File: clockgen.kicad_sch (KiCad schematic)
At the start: 146 parts, among them IC3 TLV74325PDBVR, J13 73391-0083, J14 73391-0083, J15 292161-3, J16 U.FL-R-SMT-180, Q10 BSS138, Q9 BSS138, U12 AZ1117-3.3, U13 AZ1117-3.3, U14 TCA6416APWR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

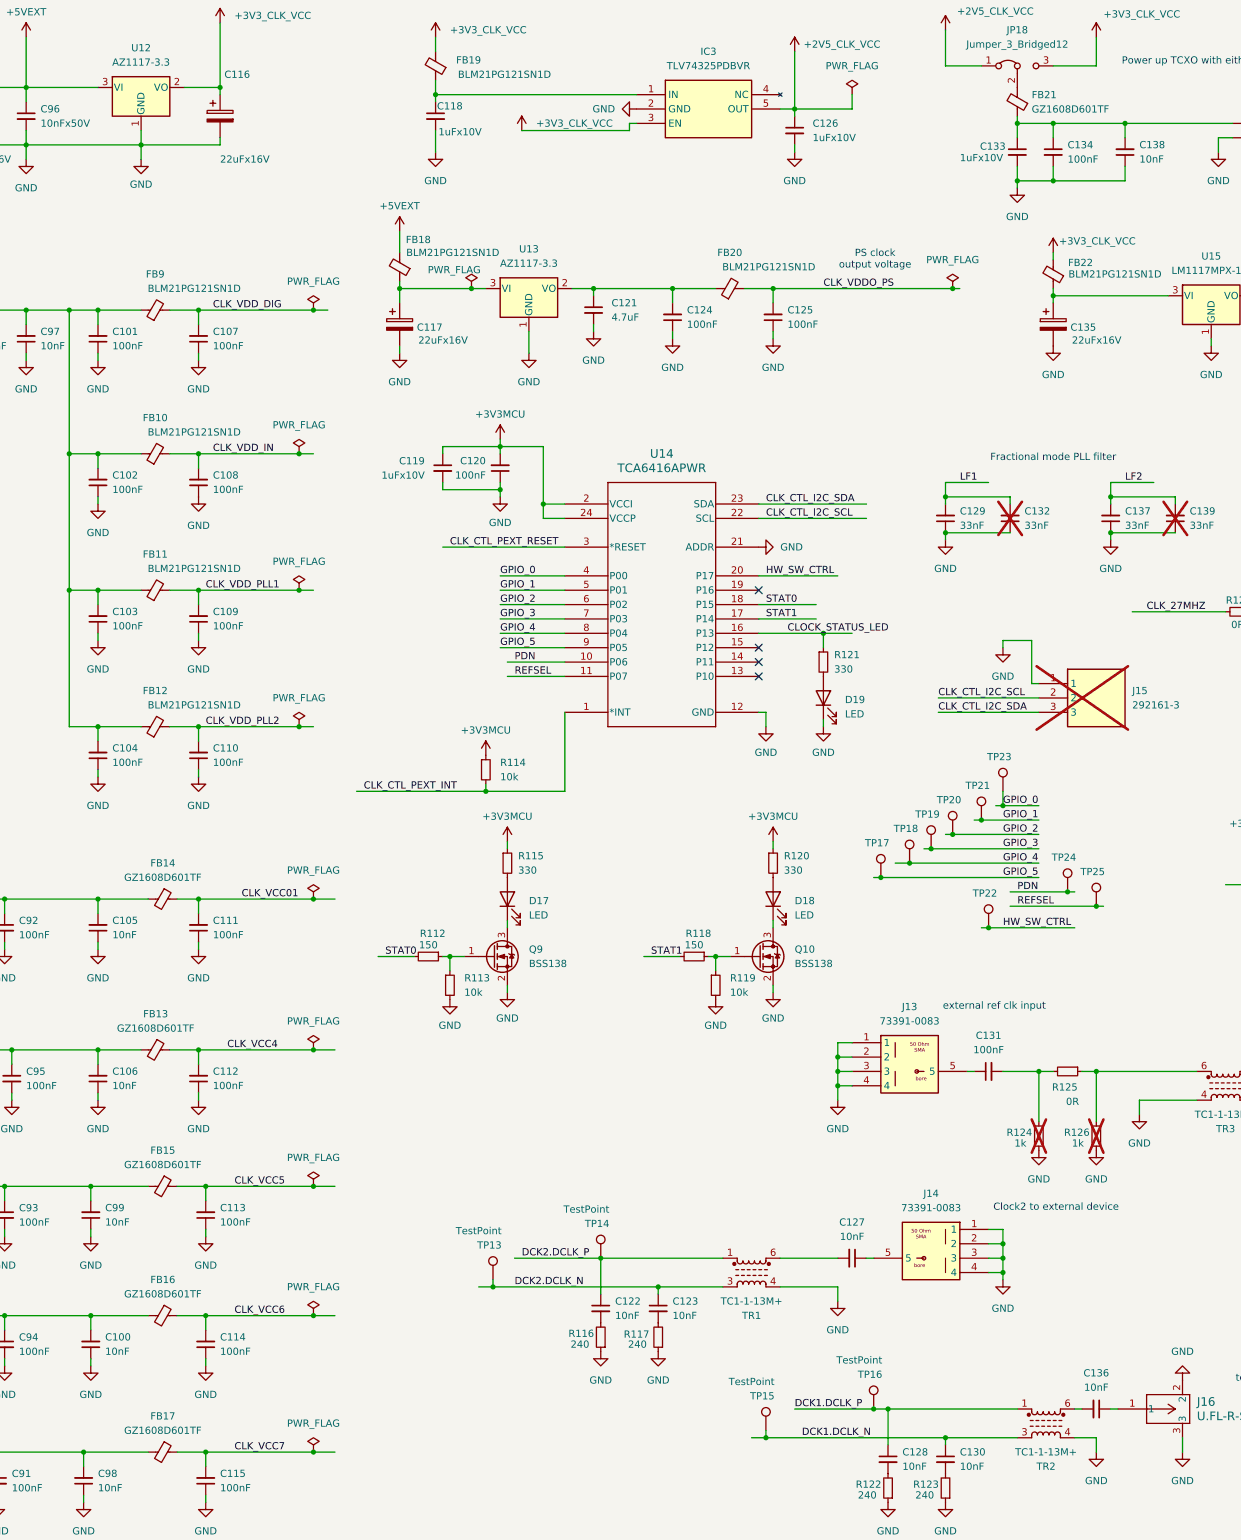
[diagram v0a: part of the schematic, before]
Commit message: JLCPCB part id's update
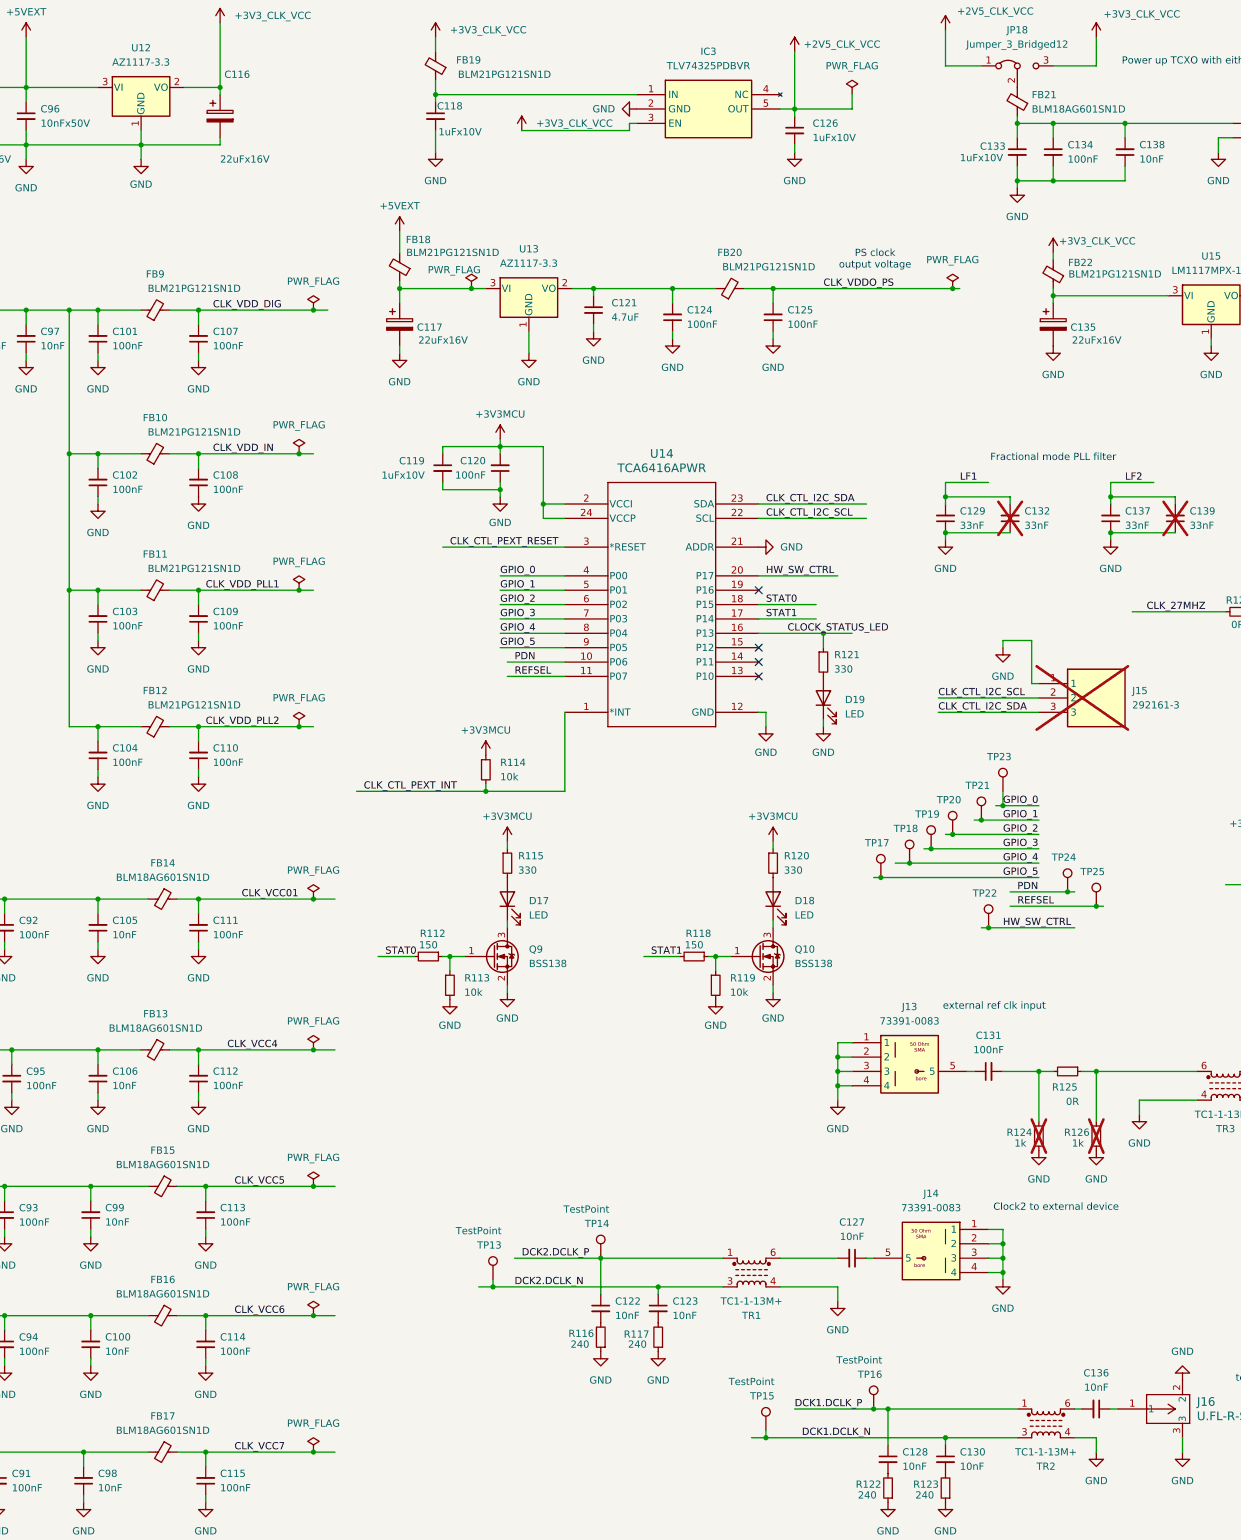
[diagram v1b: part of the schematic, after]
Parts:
- FB13, FB14, FB15, FB16, FB17, FB21: value GZ1608D601TF -> BLM18AG601SN1D; JLCPCB Part # C1002 -> C19330; Part GZ1608D601TF -> BLM18AG601SN1D
- R125, R127: JLCPCB Part # C21189 -> C2906974; Part 0603WAF0000T5E -> FRC0603F0000TS
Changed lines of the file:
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@@
 			)
 		)
-		(property "Value" "GZ1608D601TF"
+		(property "Value" "BLM18AG601SN1D"
 			(at 73.6981 167.64 90)
 			(effects
@@
 			)
 		)
-		(property "JLCPCB Part #" "C1002"
+		(property "JLCPCB Part #" "C19330"
 			(at 73.66 171.45 0)
 			(effects
@@
 			)
 		)
-		(property "Part" "GZ1608D601TF"
+		(property "Part" "BLM18AG601SN1D"
 			(at 73.66 171.45 90)
 			(effects
@@
 			)
 		)
-		(property "JLCPCB Part #" "C21189"
+		(property "JLCPCB Part #" "C2906974"
 			(at 264.16 120.65 0)
 			(effects
@@
 			)
 		)
-		(property "Part" "0603WAF0000T5E"
+		(property "Part" "FRC0603F0000TS"
 			(at 264.16 120.65 90)
 			(effects
@@
 			)
 		)
-		(property "Value" "GZ1608D601TF"
+		(property "Value" "BLM18AG601SN1D"
 			(at 73.6981 241.3 90)
 			(effects
@@
 			)
 		)
-		(property "JLCPCB Part #" "C1002"
+		(property "JLCPCB Part #" "C19330"
 			(at 73.66 245.11 0)
 			(effects
@@
 			)
 		)
-		(property "Part" "GZ1608D601TF"
+		(property "Part" "BLM18AG601SN1D"
 			(at 73.66 245.11 90)
 			(effects
@@
 			)
 		)
-		(property "Value" "GZ1608D601TF"
+		(property "Value" "BLM18AG601SN1D"
 			(at 73.6981 218.44 90)
 			(effects
@@
 			)
 		)
-		(property "JLCPCB Part #" "C1002"
+		(property "JLCPCB Part #" "C19330"
 			(at 73.66 222.25 0)
 			(effects
@@
 			)
 		)
-		(property "Part" "GZ1608D601TF"
+		(property "Part" "BLM18AG601SN1D"
 			(at 73.66 222.25 90)
 			(effects
@@
 			)
 		)
-		(property "Value" "GZ1608D601TF"
+		(property "Value" "BLM18AG601SN1D"
 			(at 72.4281 194.31 90)
 			(effects
@@
 			)
 		)
-		(property "JLCPCB Part #" "C1002"
+		(property "JLCPCB Part #" "C19330"
 			(at 72.39 198.12 0)
 			(effects
@@
 			)
 		)
-		(property "Part" "GZ1608D601TF"
+		(property "Part" "BLM18AG601SN1D"
 			(at 72.39 198.12 90)
 			(effects
@@
 			)
 		)
-		(property "Value" "GZ1608D601TF"
+		(property "Value" "BLM18AG601SN1D"
 			(at 73.6981 265.43 90)
 			(effects
@@
 			)
 		)
-		(property "JLCPCB Part #" "C1002"
+		(property "JLCPCB Part #" "C19330"
 			(at 73.66 269.24 0)
 			(effects
@@
 			)
 		)
-		(property "Part" "GZ1608D601TF"
+		(property "Part" "BLM18AG601SN1D"
 			(at 73.66 269.24 90)
 			(effects
@@
 			)
 		)
-		(property "JLCPCB Part #" "C21189"
+		(property "JLCPCB Part #" "C2906974"
 			(at 233.68 201.93 0)
 			(effects
@@
 			)
 		)
-		(property "Part" "0603WAF0000T5E"
+		(property "Part" "FRC0603F0000TS"
 			(at 233.68 201.93 90)
 			(effects
@@
 			)
 		)
-		(property "Value" "GZ1608D601TF"
+		(property "Value" "BLM18AG601SN1D"
 			(at 227.33 31.788 0)
 			(effects
@@
 			)
 		)
-		(property "JLCPCB Part #" "C1002"
+		(property "JLCPCB Part #" "C19330"
 			(at 224.79 30.48 0)
 			(effects
@@
 			)
 		)
-		(property "Part" "GZ1608D601TF"
+		(property "Part" "BLM18AG601SN1D"
 			(at 224.79 30.48 90)
 			(effects
